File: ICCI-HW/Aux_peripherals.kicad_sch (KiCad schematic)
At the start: 38 parts, among them J401 EXP0, J402 EXP1, J403 DM3AT-SF-PEJM5, Q401 RZM001P02, Q402 PDTC114Y, Q403 PDTC114Y, Q404 PDTC114Y, Q405 PDTC114Y, U401 PCF2127AT, U402 SAM-M8Q

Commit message: hw: updates
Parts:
- removed NT401: NetTie_2, NetTie:NetTie-2_SMD_Pad0.5mm, symbol Device:NetTie_2
- D402: footprint Package_DFN_QFN:UDFN-9_1.0x3.8mm_P0.5mm -> ICCI-LIB:ICCI_UDFN-9_1.0x3.8mm_P0.5mm
- J403: footprint Connector_Card:microSD_HC_Hirose_DM3AT-SF-PEJM5 -> ICCI-LIB:ICCI_microSD_HC_Hirose_DM3AT-SF-PEJM5
- U402: footprint RF_GPS:ublox_SAM-M8Q_HandSolder -> ICCI-LIB:ICCI_ublox_SAM-M8Q
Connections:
- net IFS is gone; now on net BBS: U401.5 (IFS)
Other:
- company: tollsimy -> Simone Tollardo
- moved on the sheet: BT401, C401, C404, C407, C408, C409, C410

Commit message: hw: updates
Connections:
- net ~{SD_DET}: no longer RN401.1 (R1.1)
- new net SD_DET_B: RN401.1 (R1.1)

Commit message: hw: updates
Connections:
- net +3V3: no longer C401.1, C404.1
- net GPS_VCC: now also C401.1, C404.1
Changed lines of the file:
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@@
+    (stroke (width 0) (type default) (color 0 0 0 0))
+  )
+  (wire (pts (xy 32.385 57.785) (xy 26.035 57.785))
     (stroke (width 0) (type default) (color 0 0 0 0))
   )
@@
     (stroke (width 0) (type default) (color 0 0 0 0))
   )
+  (wire (pts (xy 32.385 59.69) (xy 32.385 57.785))
+    (stroke (width 0) (type default) (color 0 0 0 0))
+  )
   (wire (pts (xy 40.005 50.165) (xy 29.845 50.165))
     (stroke (width 0) (type default) (color 0 0 0 0))
@@
   )
   (wire (pts (xy 51.435 113.03) (xy 60.96 113.03))
+    (stroke (width 0) (type default) (color 0 0 0 0))
+  )
+  (wire (pts (xy 26.035 57.785) (xy 26.035 59.69))
     (stroke (width 0) (type default) (color 0 0 0 0))
   )
@@
   )
   (label "~{SD_CS}" (at 204.47 33.655 180)
+    (effects (font (size 1.27 1.27)) (justify right bottom))
+  )
+  (label "GPS_VCC" (at 32.385 57.785 180)
     (effects (font (size 1.27 1.27)) (justify right bottom))
   )
@@
     (pin "1")
   )
-  (symbol (lib_id "power:+3V3") (at 32.385 59.69 0) (unit 1)
-    (in_bom yes) (on_board yes)
-    (property "Reference" "#PWR0410" (id 0) (at 32.385 63.5 0)
-      (effects (font (size 1.27 1.27)) hide)
-    )
-    (property "Value" "+3V3" (id 1) (at 31.75 55.88 0))
-    (property "Footprint" "" (id 2) (at 32.385 59.69 0)
-      (effects (font (size 1.27 1.27)) hide)
-    )
-    (property "Datasheet" "" (id 3) (at 32.385 59.69 0)
-      (effects (font (size 1.27 1.27)) hide)
-    )
-    (pin "1")
-  )
   (symbol (lib_id "power:GND") (at 26.67 133.985 0) (unit 1)
     (in_bom yes) (on_board yes)
@@
       (effects (font (size 1.27 1.27)) hide)
     )
-    (pin "1")
-  )
-  (symbol (lib_id "power:+3V3") (at 26.035 59.69 0) (unit 1)
-    (in_bom yes) (on_board yes)
-    (property "Reference" "#PWR0402" (id 0) (at 26.035 63.5 0)
-      (effects (font (size 1.27 1.27)) hide)
-    )
-    (property "Value" "+3V3" (id 1) (at 25.4 55.88 0))
-    (property "Footprint" "" (id 2) (at 26.035 59.69 0)
-      (effects (font (size 1.27 1.27)) hide)
-    )
-    (property "Datasheet" "" (id 3) (at 26.035 59.69 0)
-      (effects (font (size 1.27 1.27)) hide)
-    )

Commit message: start layout
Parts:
- removed J401: EXP0, Connector_PinHeader_2.54mm:PinHeader_1x04_P2.54mm_Vertical, symbol Connector:Conn_01x04_Male
- removed J402: EXP1, Connector_PinHeader_2.54mm:PinHeader_1x04_P2.54mm_Vertical, symbol Connector:Conn_01x04_Male
- added J401: EXP, Connector_PinSocket_2.54mm:PinSocket_2x03_P2.54mm_Horizontal, symbol Connector:Conn_01x06_Female
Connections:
- net SD_DET_B is gone; now on net ~{SD_DET}: RN401.1 (R1.1)
- net +3V3: now also J401.6 (Pin_6)
- net GND: now also J401.1 (Pin_1)
- net SCL0: now also J401.5 (Pin_5)
- net SCL1: now also J401.3 (Pin_3)
- net SDA0: now also J401.4 (Pin_4)
- net SDA1: now also J401.2 (Pin_2)

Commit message: layout updates
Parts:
- removed J401: EXP, Connector_PinSocket_2.54mm:PinSocket_2x03_P2.54mm_Horizontal, symbol Connector:Conn_01x06_Female
- added J401: EXP, Connector_PinSocket_2.54mm:PinSocket_2x02_P2.54mm_Horizontal, symbol Connector:Conn_01x04_Female
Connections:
- net +3V3: now also J401.4 (Pin_4)
- net GND: now also J401.1 (Pin_1)
- net SCL0: now also J401.3 (Pin_3)
- net SDA0: now also J401.2 (Pin_2)
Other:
- note added: "I2C Expansion"
- note removed: "I2C Expansions"
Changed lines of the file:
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@@
     (stroke (width 0) (type default) (color 0 0 0 0))
   )
-  (wire (pts (xy 38.735 172.085) (xy 38.735 172.72))
+  (wire (pts (xy 38.735 168.91) (xy 38.735 169.545))
     (stroke (width 0) (type default) (color 0 0 0 0))
   )
@@
     (stroke (width 0) (type default) (color 0 0 0 0))
   )
-  (wire (pts (xy 36.83 164.465) (xy 43.18 164.465))
+  (wire (pts (xy 36.83 166.37) (xy 43.18 166.37))
     (stroke (width 0) (type default) (color 0 0 0 0))
   )
@@
     (stroke (width 0) (type default) (color 0 0 0 0))
   )
-  (wire (pts (xy 36.83 169.545) (xy 43.18 169.545))
-    (stroke (width 0) (type default) (color 0 0 0 0))
-  )
   (wire (pts (xy 56.515 120.65) (xy 60.96 120.65))
     (stroke (width 0) (type default) (color 0 0 0 0))
@@
     (stroke (width 0) (type default) (color 0 0 0 0))
   )
-  (wire (pts (xy 36.83 161.925) (xy 43.18 161.925))
+  (wire (pts (xy 36.83 163.83) (xy 43.18 163.83))
     (stroke (width 0) (type default) (color 0 0 0 0))
   )
@@
     (stroke (width 0) (type default) (color 0 0 0 0))
   )
-  (wire (pts (xy 36.83 172.085) (xy 38.735 172.085))
+  (wire (pts (xy 36.83 168.91) (xy 38.735 168.91))
     (stroke (width 0) (type default) (color 0 0 0 0))
   )
@@
     (stroke (width 0) (type default) (color 0 0 0 0))
   )
-  (wire (pts (xy 38.735 158.75) (xy 38.735 159.385))
+  (wire (pts (xy 38.735 160.655) (xy 38.735 161.29))
     (stroke (width 0) (type default) (color 0 0 0 0))
   )
@@
     (stroke (width 0) (type default) (color 0 0 0 0))
   )
-  (wire (pts (xy 38.735 159.385) (xy 36.83 159.385))
+  (wire (pts (xy 38.735 161.29) (xy 36.83 161.29))
     (stroke (width 0) (type default) (color 0 0 0 0))
   )
@@
   )
   (wire (pts (xy 78.74 38.735) (xy 78.74 36.195))
-    (stroke (width 0) (type default) (color 0 0 0 0))
-  )
-  (wire (pts (xy 36.83 167.005) (xy 43.18 167.005))
     (stroke (width 0) (type default) (color 0 0 0 0))
   )
@@
     (effects (font (size 3 3) (thickness 0.6) bold) (justify right bottom))
   )
-  (text "I2C Expansions" (at 57.15 148.59 180)
+  (text "I2C Expansion" (at 56.515 150.495 180)
     (effects (font (size 3 3) (thickness 0.6) bold) (justify right bottom))
   )
@@
     (effects (font (size 1.27 1.27)) (justify right bottom))
   )
-  (label "SCL1" (at 42.545 167.005 180)
-    (effects (font (size 1.27 1.27)) (justify right bottom))
-  )
   (label "SD_DAT1" (at 204.47 43.815 180)
     (effects (font (size 1.27 1.27)) (justify right bottom))
   )
-  (label "SCL0" (at 42.545 161.925 180)
+  (label "SCL0" (at 42.545 163.83 180)
     (effects (font (size 1.27 1.27)) (justify right bottom))
   )
@@
     (effects (font (size 1.27 1.27)) (justify right bottom))
   )
-  (label "SDA1" (at 42.545 169.545 180)
-    (effects (font (size 1.27 1.27)) (justify right bottom))
-  )
-  (label "SDA0" (at 42.545 164.465 180)
+  (label "SDA0" (at 42.545 166.37 180)
     (effects (font (size 1.27 1.27)) (justify right bottom))
   )
@@
     (effects (font (size 1.27 1.27)) (justify left))
   )
-  (hierarchical_label "SCL0" (shape input) (at 43.18 161.925 0)
+  (hierarchical_label "SCL0" (shape input) (at 43.18 163.83 0)
     (effects (font (size 1.27 1.27)) (justify left))
   )
@@
     (effects (font (size 1.27 1.27)) (justify right))
   )
-  (hierarchical_label "SCL1" (shape input) (at 43.18 167.005 0)
-    (effects (font (size 1.27 1.27)) (justify left))
-  )
   (hierarchical_label "LED_R" (shape input) (at 222.25 125.73 90)
     (effects (font (size 1.27 1.27)) (justify left))
@@
     (effects (font (size 1.27 1.27)) (justify right))
   )
-  (hierarchical_label "SDA0" (shape bidirectional) (at 43.18 164.465 0)
+  (hierarchical_label "SDA0" (shape bidirectional) (at 43.18 166.37 0)
     (effects (font (size 1.27 1.27)) (justify left))
   )
@@
   (hierarchical_label "GPS_EXTINT" (shape input) (at 52.705 48.895 180)
     (effects (font (size 1.27 1.27)) (justify right))
-  )
-  (hierarchical_label "SDA1" (shape bidirectional) (at 43.18 169.545 0)
-    (effects (font (size 1.27 1.27)) (justify left))
   )
   (hierarchical_label "RTC_CLKOUT" (shape output) (at 100.33 113.03 0)
@@
     (pin "1")
   )
-  (symbol (lib_id "Connector:Conn_01x06_Female") (at 31.75 167.005 180) (unit 1)
-    (in_bom yes) (on_board yes)
-    (property "Reference" "J401" (id 0) (at 25.4 163.83 0))
-    (property "Value" "EXP" (id 1) (at 25.4 166.37 0))
-    (property "Footprint" "Connector_PinSocket_2.54mm:PinSocket_2x03_P2.54mm_Horizontal" (id 2) (at 31.75 167.005 0)
-      (effects (font (size 1.27 1.27)) hide)
-    )
-    (property "Datasheet" "~" (id 3) (at 31.75 167.005 0)
-      (effects (font (size 1.27 1.27)) hide)
-    )
-    (pin "1")
-    (pin "2")
-    (pin "3")
-    (pin "4")
-    (pin "5")
-    (pin "6")
-  )
   (symbol (lib_id "power:PWR_FLAG") (at 50.8 36.195 0) (unit 1)
     (in_bom yes) (on_board yes)
@@
     (pin "3")
   )
-  (symbol (lib_id "power:+3V3") (at 38.735 158.75 0) (unit 1)
-    (in_bom yes) (on_board yes)
-    (property "Reference" "#PWR0408" (id 0) (at 38.735 162.56 0)
-      (effects (font (size 1.27 1.27)) hide)
-    )
-    (property "Value" "+3V3" (id 1) (at 38.1 154.94 0))
-    (property "Footprint" "" (id 2) (at 38.735 158.75 0)
-      (effects (font (size 1.27 1.27)) hide)
-    )
-    (property "Datasheet" "" (id 3) (at 38.735 158.75 0)
+  (symbol (lib_id "power:+3V3") (at 38.735 160.655 0) (unit 1)
+    (in_bom yes) (on_board yes)
+    (property "Reference" "#PWR0408" (id 0) (at 38.735 164.465 0)
+      (effects (font (size 1.27 1.27)) hide)
+    )
+    (property "Value" "+3V3" (id 1) (at 38.1 156.845 0))
+    (property "Footprint" "" (id 2) (at 38.735 160.655 0)
+      (effects (font (size 1.27 1.27)) hide)
+    )
+    (property "Datasheet" "" (id 3) (at 38.735 160.655 0)
       (effects (font (size 1.27 1.27)) hide)
     )
@@
     (pin "2")
   )
-  (symbol (lib_id "power:GND") (at 38.735 172.72 0) (unit 1)
-    (in_bom yes) (on_board yes)
-    (property "Reference" "#PWR0409" (id 0) (at 38.735 179.07 0)
-      (effects (font (size 1.27 1.27)) hide)
-    )
-    (property "Value" "GND" (id 1) (at 38.735 176.53 0))
-    (property "Footprint" "" (id 2) (at 38.735 172.72 0)
-      (effects (font (size 1.27 1.27)) hide)
-    )
-    (property "Datasheet" "" (id 3) (at 38.735 172.72 0)
+  (symbol (lib_id "power:GND") (at 38.735 169.545 0) (unit 1)
+    (in_bom yes) (on_board yes)
+    (property "Reference" "#PWR0409" (id 0) (at 38.735 175.895 0)
+      (effects (font (size 1.27 1.27)) hide)
+    )
+    (property "Value" "GND" (id 1) (at 38.735 173.355 0))
+    (property "Footprint" "" (id 2) (at 38.735 169.545 0)
+      (effects (font (size 1.27 1.27)) hide)
+    )
+    (property "Datasheet" "" (id 3) (at 38.735 169.545 0)
       (effects (font (size 1.27 1.27)) hide)
     )
@@
     (pin "2")
   )
+  (symbol (lib_id "Connector:Conn_01x04_Female") (at 31.75 166.37 180) (unit 1)
+    (in_bom yes) (on_board yes)
+    (property "Reference" "J401" (id 0) (at 27.305 163.83 0))
+    (property "Value" "EXP" (id 1) (at 27.94 166.37 0))
+    (property "Footprint" "Connector_PinSocket_2.54mm:PinSocket_2x02_P2.54mm_Horizontal" (id 2) (at 31.75 166.37 0)
+      (effects (font (size 1.27 1.27)) hide)
+    )
+    (property "Datasheet" "~" (id 3) (at 31.75 166.37 0)
+      (effects (font (size 1.27 1.27)) hide)
+    )
+    (pin "1")
+    (pin "2")
+    (pin "3")
+    (pin "4")
+  )
   (symbol (lib_id "power:GND") (at 279.4 59.055 0) (unit 1)

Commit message: layout PCB V1.0
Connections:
- net ~{GPS_RESET} renamed ~{GPS_RST}
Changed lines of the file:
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@@
     (title "AUX + Peripherals")
     (date "2022-07-14")
-    (rev "BETA")
+    (rev "1.0")
     (company "Simone Tollardo")
   )
@@
     (effects (font (size 1.27 1.27)) (justify right bottom))
   )
-  (label "~{GPS_RESET}" (at 52.705 56.515 0)
+  (label "~{GPS_RST}" (at 52.705 56.515 0)
     (effects (font (size 1.27 1.27)) (justify left bottom))
   )
@@
     (effects (font (size 1.27 1.27)) (justify left))
   )
-  (hierarchical_label "~{GPS_RESET}" (shape input) (at 52.705 56.515 180)
+  (hierarchical_label "~{GPS_RST}" (shape input) (at 52.705 56.515 180)
     (effects (font (size 1.27 1.27)) (justify right))
   )

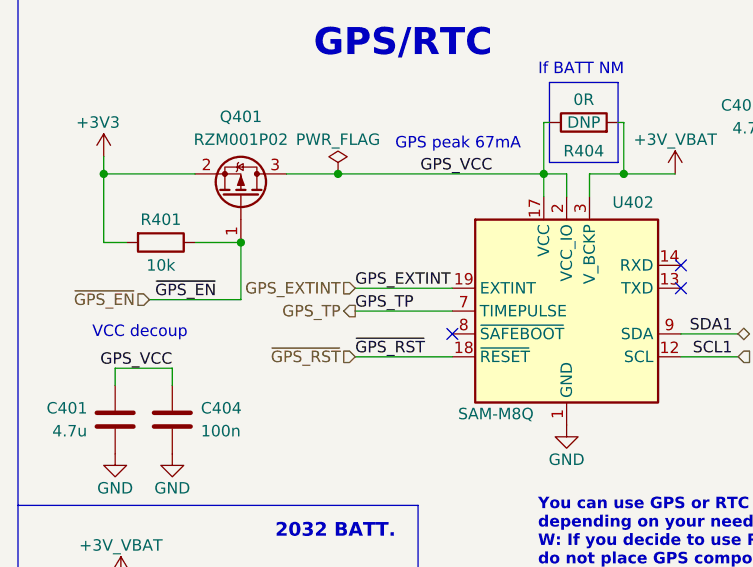
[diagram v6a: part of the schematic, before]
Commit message: hw: fix missing contact from SYS to SYSA on MAX77960
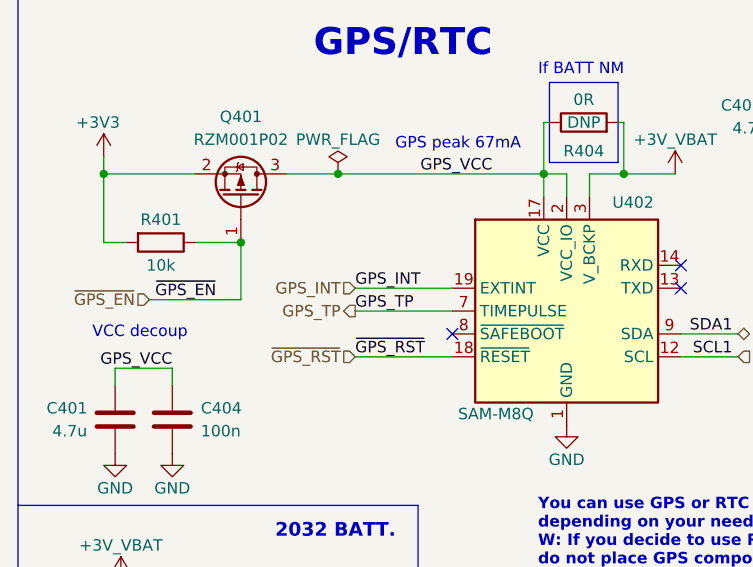
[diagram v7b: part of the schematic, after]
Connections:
- net GPS_EXTINT renamed GPS_INT
